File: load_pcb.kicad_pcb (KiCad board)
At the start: 2 copper layers, 32 parts, among them J1 Conn_01x16, J2 Conn_01x08, J3 Conn_01x10, P1 282837-2, P2 282837-2, P3 282837-2, P4 282837-2, Q1 BC846BPDW1, Q2 IRFP064V, Q3 IRFP064V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

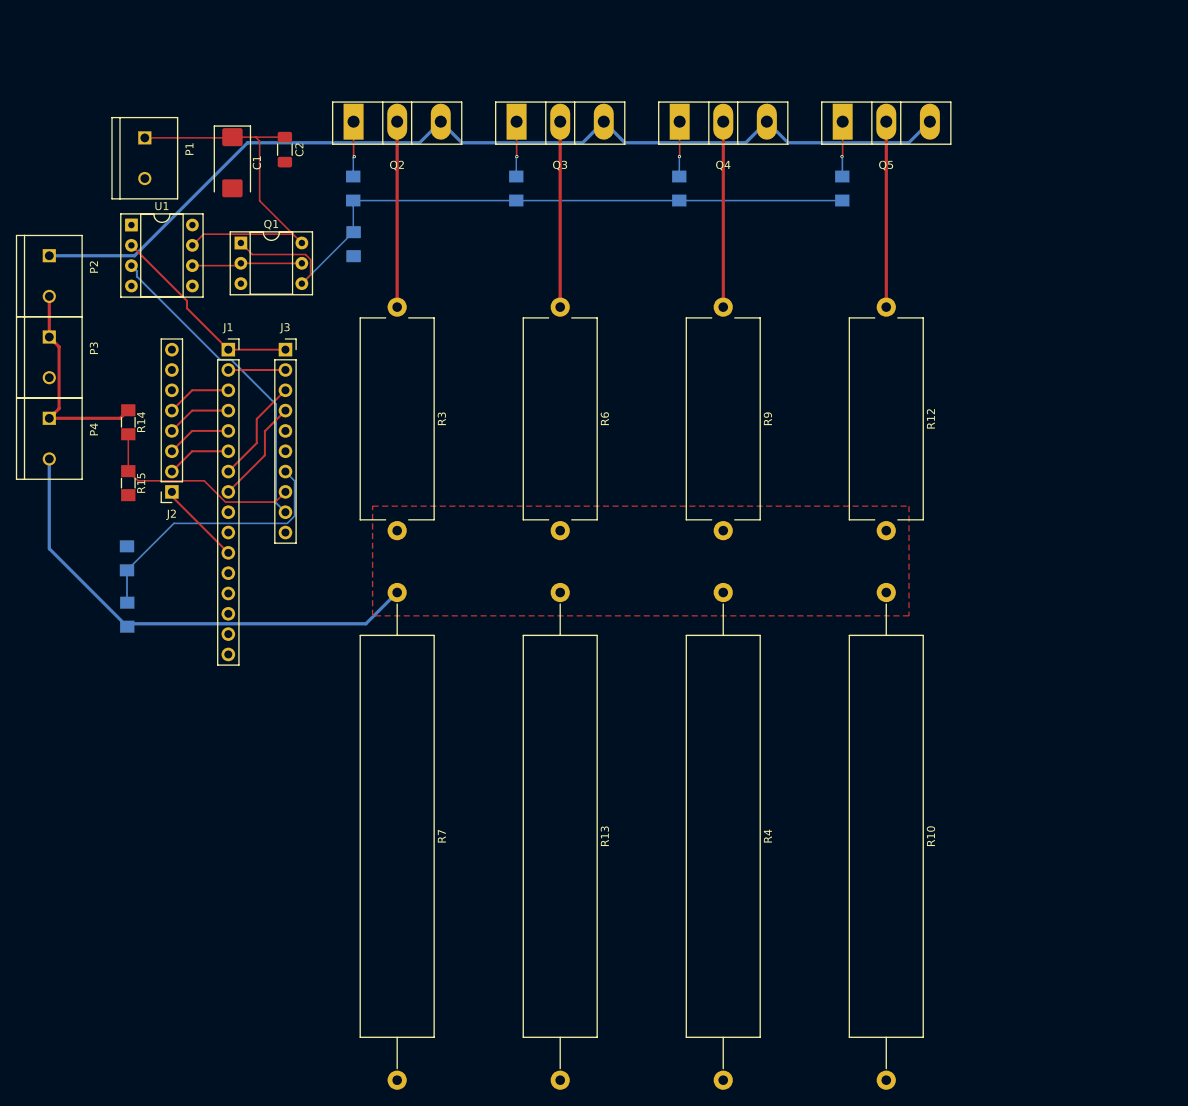
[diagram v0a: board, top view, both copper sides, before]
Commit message: Changed positions of connectors
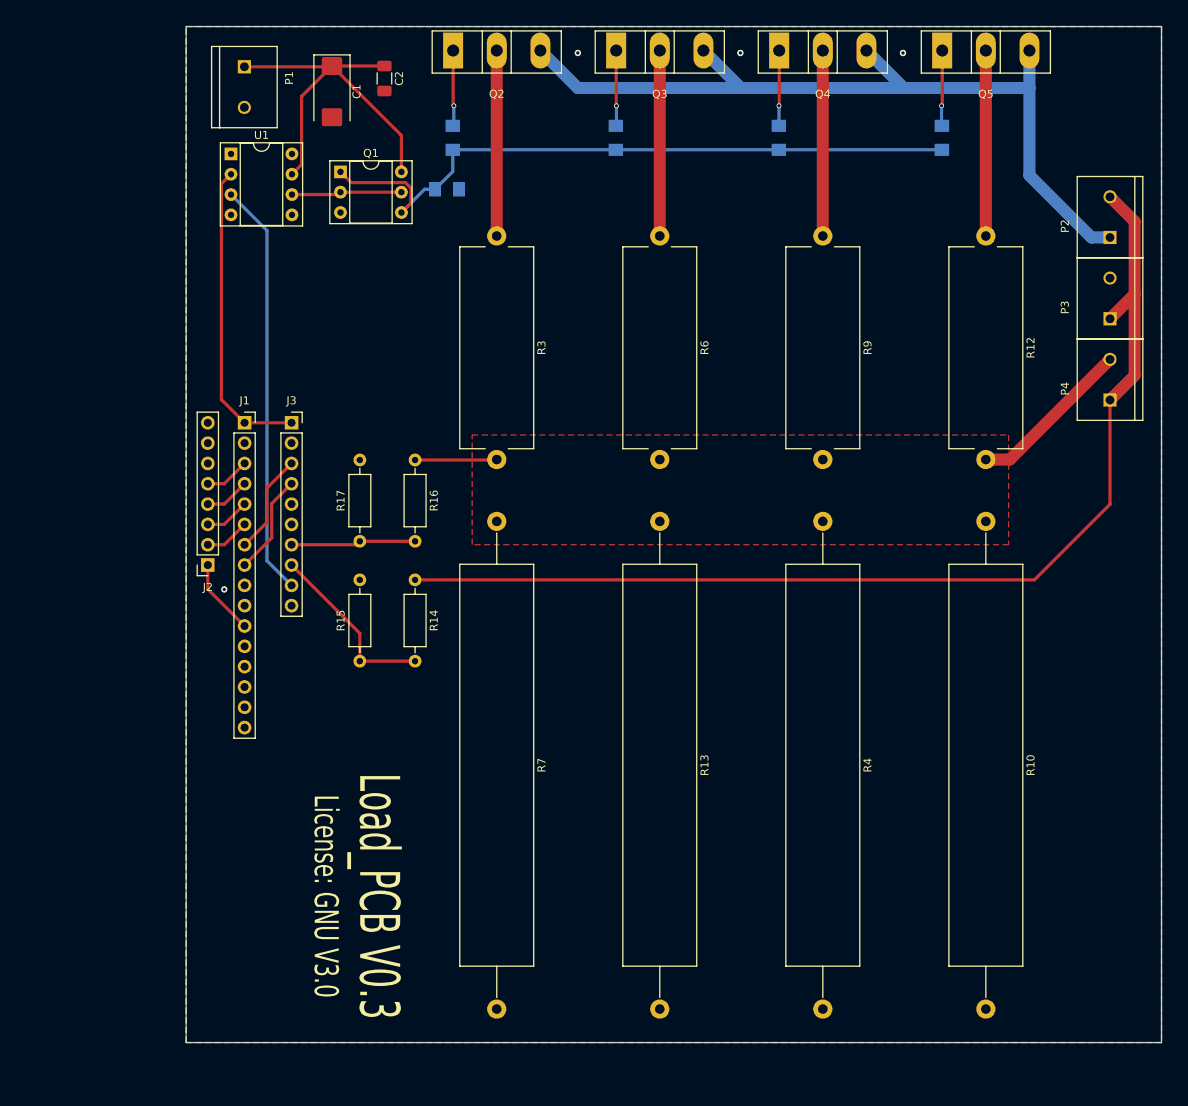
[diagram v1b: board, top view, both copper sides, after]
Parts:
- R14, R15: footprint Resistor_SMD:R_MiniMELF_MMA-0204 -> Resistor_THT:R_Axial_DIN0207_L6.3mm_D2.5mm_P10.16mm_Horizontal
- R16, R17: footprint Resistor_SMD:R_MiniMELF_MMA-0204 -> Resistor_THT:R_Axial_DIN0207_L6.3mm_D2.5mm_P10.16mm_Horizontal; moved to F.Cu
- moved P2 132.8 mm to (216.1, 50.5), turned to 90 degrees
- moved P3 132.8 mm to (216.1, 60.7), turned to 90 degrees
- moved P4 132.8 mm to (216.1, 70.8), turned to 90 degrees
- moved R14 40.9 mm to (129.3, 95.8)
- moved R16 40.8 mm to (129.3, 80.8), turned to -90 degrees
- moved R15 36.5 mm to (122.4, 106.0), turned to 90 degrees
- moved R17 29.2 mm to (122.4, 91.0)
- moved Q3 15.3 mm to (154.4, 29.7)
- moved P1 15.3 mm to (107.9, 34.2)
- moved Q2 15.3 mm to (134.0, 29.7)
- moved C1 15.3 mm to (118.9, 34.8)
- moved C2 15.3 mm to (125.4, 33.2)
- moved Q4 15.3 mm to (174.8, 29.7)
- moved Q5 15.3 mm to (195.2, 29.7)
- moved R10 15.3 mm to (200.6, 88.5)
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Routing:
- net Net-(P2-Pad2): track 26.5 -> 136.1 mm
- net All_R: track 60.5 -> 30.9 mm
- net Net-(P2-Pad1): track 123.6 -> 105.2 mm
- net DIV1: track 33.9 -> 15.6 mm
- net Net-(J1-Pad1): track 25.2 -> 38.6 mm
- net OPAMP+: track 39.6 -> 52.0 mm
- net GND: track 7.14 -> 0.00 mm, vias 0 -> 4
- net DIV2: track 26.4 -> 22.5 mm
- net +12V: track 46.3 -> 50.0 mm
- net Net-(Q5-Pad1): track 6.92 -> 9.46 mm
- net Net-(Q4-Pad1): track 6.88 -> 9.42 mm
- net Net-(Q2-Pad1): track 6.96 -> 9.50 mm
- net Net-(Q3-Pad1): track 6.91 -> 9.45 mm
- net Net-(J1-Pad6): track 8.11 -> 5.65 mm
- net Net-(J1-Pad3): track 8.11 -> 5.65 mm
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- added copper zone on B.Cu, net GND
- added copper zone on F.Cu, net GND
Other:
- board outline added: 121.9 x 127 mm
- board text added: "License: GNU V3.0"
- board text added: "Load_PCB V0.3"

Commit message: Added DAC and corrected positions of SMD/THD
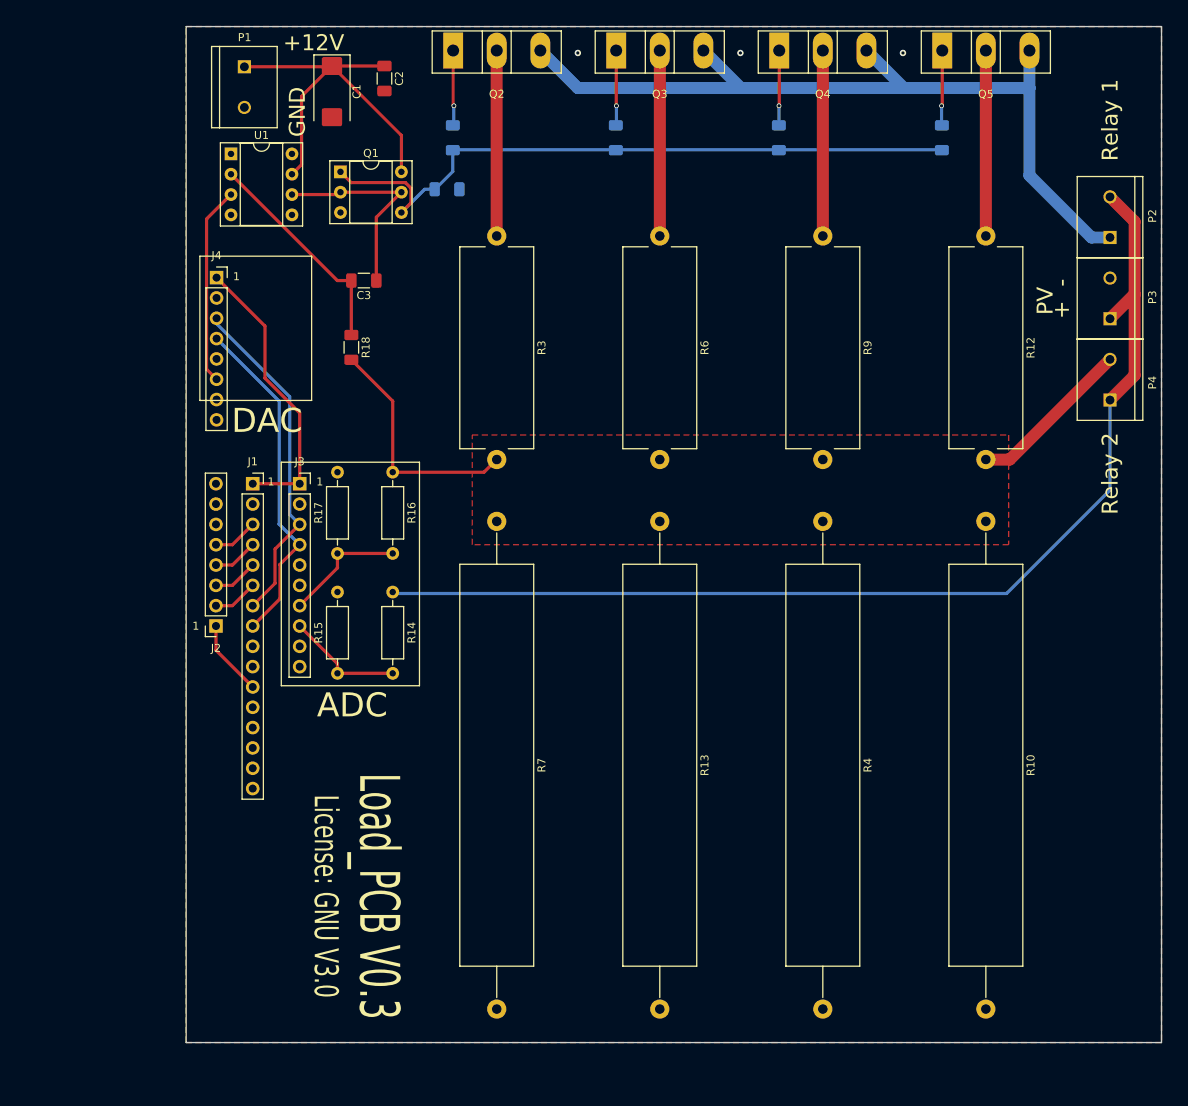
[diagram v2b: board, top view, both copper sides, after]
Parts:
- added C3: 100p, Capacitor_SMD:C_1206_3216Metric_Pad1.33x1.80mm_HandSolder, F.Cu at (122.9, 58.4)
- added J4: Conn_01x08, Connector_PinSocket_2.54mm:PinSocket_1x08_P2.54mm_Vertical, F.Cu at (104.4, 58.1)
- added R18: 10k, Resistor_SMD:R_1206_3216Metric_Pad1.30x1.75mm_HandSolder, F.Cu at (121.3, 66.8)
- R1, R11, R2, R5, R8: footprint Resistor_SMD:R_MiniMELF_MMA-0204 -> Resistor_SMD:R_1206_3216Metric_Pad1.30x1.75mm_HandSolder
- moved J2 7.69 mm to (104.4, 101.6)
- moved J3 7.69 mm to (114.8, 83.8)
- moved J1 7.69 mm to (109.0, 83.8)
- moved R14 3.18 mm to (126.5, 97.4)
- moved R15 3.18 mm to (119.6, 107.5)
- moved R16 3.18 mm to (126.5, 82.4)
- moved R17 3.18 mm to (119.6, 92.5)
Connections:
- net Net-(J1-Pad7) renamed /(28) SCL
- net Net-(J1-Pad8) renamed /(27) SDA
- J1 pad 1: Net-(J1-Pad1) -> /(02) 5V
- J1 pad 3: Net-(J1-Pad3) -> /???
- J1 pad 4: Net-(J1-Pad4) -> /???
- J1 pad 5: Net-(J1-Pad5) -> /???
- J1 pad 6: Net-(J1-Pad6) -> /???
- J2 pad 2: Net-(J1-Pad6) -> /???
- J2 pad 3: Net-(J1-Pad5) -> /???
- J2 pad 4: Net-(J1-Pad4) -> /???
- J2 pad 5: Net-(J1-Pad3) -> /???
- J3 pad 1: Net-(J1-Pad1) -> /(02) 5V
- J3 pad 9: OPAMP+ -> unconnected-(J3-Pad9)
- U1 pad 2: Net-(J1-Pad1) -> Net-(U1-Pad2)
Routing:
- net Net-(J1-Pad1): track 38.6 -> 0.00 mm
- net /(02) 5V: track 0.00 -> 35.9 mm
- net /(28) SCL: track 12.6 -> 42.7 mm
- net /(27) SDA: track 12.6 -> 42.7 mm
- net Net-(U1-Pad2): track 0.00 -> 27.4 mm
- net OPAMP+: track 52.0 -> 24.9 mm
- net /???: track 0.00 -> 22.6 mm
- net All_R: track 30.9 -> 50.6 mm
- net Net-(Q1-Pad2): track 13.8 -> 26.1 mm
- net DIV2: track 22.5 -> 14.8 mm
- net Net-(J1-Pad5): track 5.65 -> 0.00 mm
- net Net-(J1-Pad4): track 5.65 -> 0.00 mm
- net Net-(J1-Pad6): track 5.65 -> 0.00 mm
- net Net-(J1-Pad3): track 5.65 -> 0.00 mm
- net Net-(P2-Pad2): track 136.1 -> 138.6 mm
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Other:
- board text added: "+ -"
- board text added: "+12V"
- board text added: "1"
- board text added: "ADC"
- board text added: "DAC"
- board text added: "GND"
- board text added: "PV"
- board text added: "Relay 1"
- board text added: "Relay 2"

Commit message: Small changes
Corrected values of resistors in voltage dividers and added overvoltage protection for ADC inputs.
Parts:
- added D1: 1N4733A, Diode_THT:D_DO-41_SOD81_P3.81mm_Vertical_AnodeUp, F.Cu at (129.3, 122.7)
- added D2: 1N4733A, Diode_THT:D_DO-41_SOD81_P3.81mm_Vertical_AnodeUp, F.Cu at (116.5, 122.7)
- added R19: 100 1W, Resistor_THT:R_Axial_DIN0309_L9.0mm_D3.2mm_P15.24mm_Horizontal, F.Cu at (115.2, 117.1)
- added R20: 100 1W, Resistor_THT:R_Axial_DIN0309_L9.0mm_D3.2mm_P15.24mm_Horizontal, F.Cu at (130.5, 128.4)
- R14: value 62k -> 9k1
- R15: value 62k -> 1k
- R16: value 62k -> 6k6
- R17: value 62k -> 3k3
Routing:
- net Net-(P2-Pad2): track 138.6 -> 174.7 mm, vias 0 -> 5
- net DIV2: track 14.8 -> 39.9 mm
- net All_R: track 50.6 -> 71.3 mm, vias 0 -> 3
- net DIV1: track 15.4 -> 34.6 mm
- net Net-(D2-Pad1): track 0.00 -> 6.24 mm
- net Net-(D1-Pad1): track 0.00 -> 6.11 mm
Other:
- board text added: "Raspberry Pi"

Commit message: Add a simulation in LTspice and production files
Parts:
- added F1: 10A gPV, proj_lib:Fuse_gPV_10.3x38mm, F.Cu at (215.3, 108.1)
- added R21: 36k, Resistor_THT:R_Axial_DIN0207_L6.3mm_D2.5mm_P10.16mm_Horizontal, F.Cu at (120.9, 56.9)
- C2: value 200n -> 100n
- R1, R11, R2, R5, R8: footprint Resistor_SMD:R_1206_3216Metric_Pad1.30x1.75mm_HandSolder -> Resistor_THT:R_Axial_DIN0207_L6.3mm_D2.5mm_P10.16mm_Horizontal; moved to F.Cu
- R18: footprint Resistor_SMD:R_1206_3216Metric_Pad1.30x1.75mm_HandSolder -> Resistor_THT:R_Axial_DIN0207_L6.3mm_D2.5mm_P10.16mm_Horizontal
- U1: value TL071 -> LM358; footprint Package_DIP:DIP-8_W7.62mm_Socket -> Package_DIP:DIP-8_W7.62mm_Socket_LongPads
- moved R11 6.86 mm to (195.2, 47.4)
- moved R2 6.86 mm to (134.0, 47.4)
- moved R5 6.86 mm to (154.4, 47.4)
- moved R8 6.86 mm to (174.8, 47.4)
- moved R1 6.72 mm to (131.1, 53.4), turned to 180 degrees
- moved C3 3.56 mm to (122.9, 62.0)
- moved Q1 1.80 mm to (121.2, 43.6)
- moved U1 1.15 mm to (105.9, 43.7)
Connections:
- P2 pad 2: Net-(P2-Pad2) -> Net-(F1-Pad1)
- P3 pad 1: Net-(P2-Pad2) -> Net-(F1-Pad2)
- P4 pad 1: Net-(P2-Pad2) -> Net-(F1-Pad1)
- R14 pad 1: Net-(P2-Pad2) -> Net-(F1-Pad1)
- U1 pad 1: unconnected-(U1-Pad1) -> Net-(C3-Pad1)
- U1 pad 5: unconnected-(U1-Pad5) -> GND
- U1 pad 6: Net-(C3-Pad1) -> GND
- U1 pad 7: +12V -> unconnected-(U1-Pad7)
- U1 pad 8: unconnected-(U1-Pad8) -> +12V
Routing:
- net Net-(F1-Pad1): track 0.00 -> 190.0 mm
- net Net-(P2-Pad2): track 174.7 -> 0.00 mm, vias 5 -> 0
- net Net-(F1-Pad2): track 0.00 -> 41.5 mm
- net All_R: track 71.3 -> 42.0 mm, vias 3 -> 0
- net Net-(C3-Pad1): track 26.1 -> 37.8 mm
- net GND: track 0.00 -> 5.87 mm
- net Net-(C3-Pad2): track 27.4 -> 32.2 mm
- net +12V: track 50.0 -> 45.2 mm
- net Net-(Q2-Pad1): track 9.50 -> 7.60 mm, vias 1 -> 0
- net Net-(Q5-Pad1): track 9.46 -> 7.60 mm, vias 1 -> 0
- net Net-(Q3-Pad1): track 9.45 -> 7.60 mm, vias 1 -> 0
- net Net-(Q4-Pad1): track 9.42 -> 7.60 mm, vias 1 -> 0
- net OPAMP+: track 24.9 -> 24.1 mm
- net Net-(Q1-Pad1): track 86.2 -> 85.7 mm
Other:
- board size 121.9 x 127 mm -> 123.2 x 128.3 mm
- board text added: "10x38mm"
